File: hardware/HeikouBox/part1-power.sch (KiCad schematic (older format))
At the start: 14 parts, among them J101 Barrel_Jack_Switch, U101 LD1117S33TR, U102 LD1117S25TR, U103 LD1117S12TR

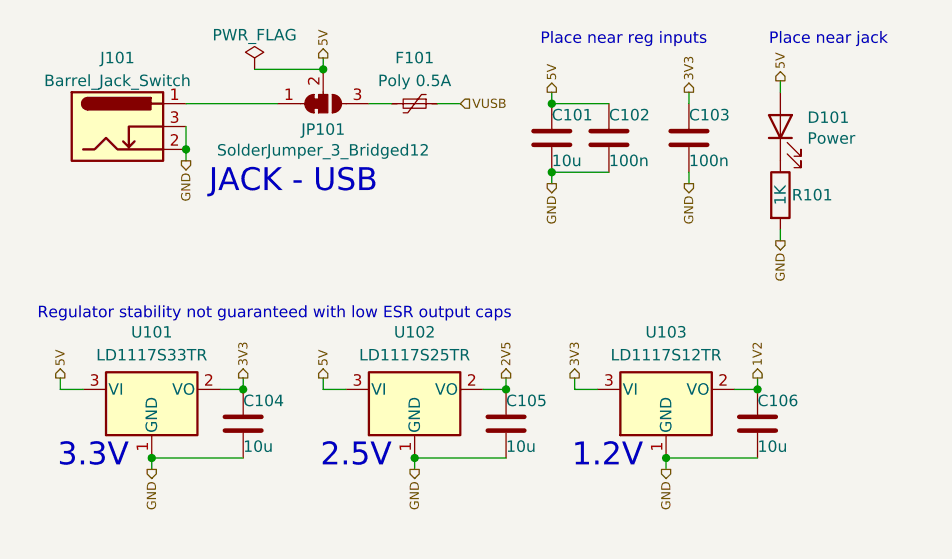
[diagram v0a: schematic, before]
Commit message: Replace MCU with blue pill, tidy up
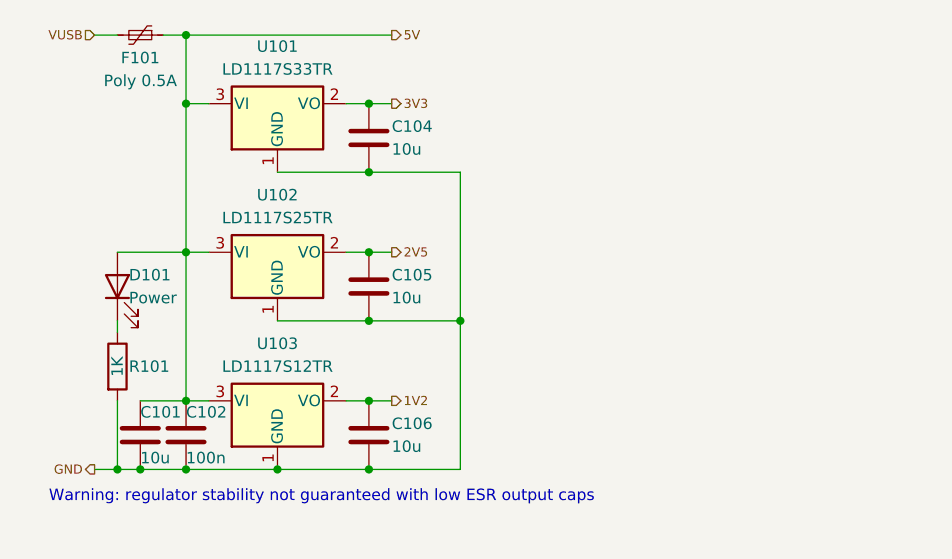
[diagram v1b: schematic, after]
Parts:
- removed C103: 100n, Capacitor_SMD:C_0603_1608Metric_Pad1.05x0.95mm_HandSolder, symbol Device:C
- removed J101: Barrel_Jack_Switch, KSK_HeikouBox:BarrelJack_Multi, symbol Connector:Barrel_Jack_Switch
- removed JP101: SolderJumper_3_Bridged12, Jumper:SolderJumper-3_P1.3mm_Bridged12_Pad1.0x1.5mm, symbol Jumper:SolderJumper_3_Bridged12
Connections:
- net 3V3: no longer U103.3 (VI)
- net 5V: now also F101.1, U103.3 (VI)
- net VUSB: now also F101.2; no longer F101.1
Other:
- note added: "Warning: regulator stability not guaranteed with low ESR output caps"
- note removed: "1.2V"
- note removed: "2.5V"
- note removed: "3.3V"
- note removed: "JACK - USB"
- note removed: "Place near jack"
- note removed: "Place near reg inputs"
- note removed: "Regulator stability not guaranteed with low ESR output caps"
- moved on the sheet: C101, C102, C104, C105, C106, D101, F101, R101, U101, U102, U103

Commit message: Fix DRC, make netlist
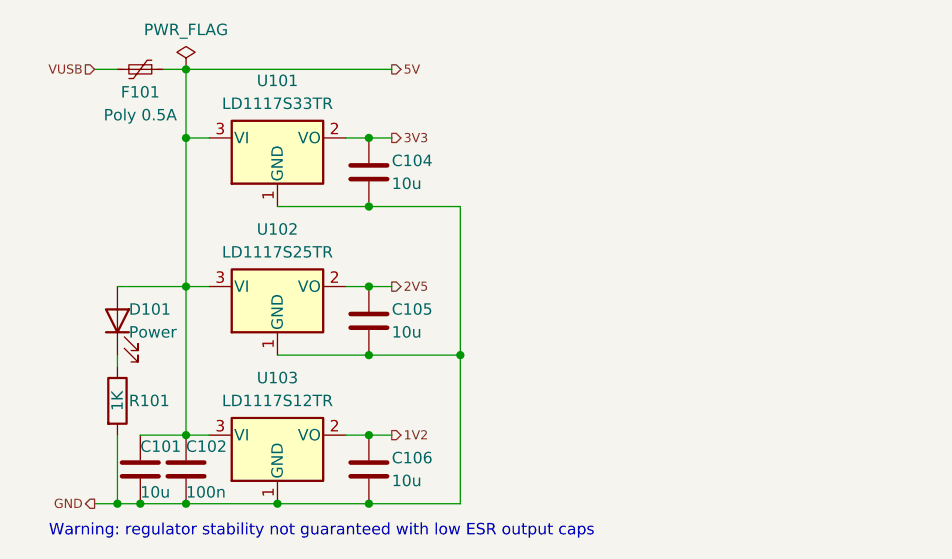
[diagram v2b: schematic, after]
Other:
- moved on the sheet: C101, C102, C104, C105, C106, D101, F101, R101, U101, U102, U103
